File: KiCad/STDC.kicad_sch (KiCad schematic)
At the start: 20 parts, among them J1 TC2030, U1 STM32L476RGTx, X1 Q13FC1350000400

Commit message: Implement Comments, Working on PCB Layout
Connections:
- net Power+Battery/Batt_Status_SCL: now reaches U1.8 (PC0)
- net BAT_STATUS_HDQ renamed Power+Battery/Batt_Status_SDA
- no-connect marks 24 -> 23
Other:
- sheet Power+Battery ports: added Batt_Status_SCL, Batt_Status_SDA; removed BATT_STATUS_HDQ
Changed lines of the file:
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@@
 	)
 	(no_connect
-		(at 130.81 68.58)
-	)
-	(no_connect
 		(at 130.81 76.2)
 	)
@@
 	(wire
 		(pts
-			(xy 85.09 86.36) (xy 105.41 86.36)
+			(xy 85.09 86.36) (xy 106.68 86.36)
 		)
 		(stroke
@@
 	(wire
 		(pts
+			(xy 85.09 83.82) (xy 104.14 83.82)
+		)
+		(stroke
+			(width 0)
+			(type default)
+		)
+	)
+	(wire
+		(pts
 			(xy 130.81 106.68) (xy 119.38 106.68)
 		)
@@
 	(wire
 		(pts
-			(xy 130.81 88.9) (xy 85.09 88.9)
+			(xy 85.09 88.9) (xy 130.81 88.9)
 		)
 		(stroke
@@
 	(wire
 		(pts
-			(xy 105.41 71.12) (xy 130.81 71.12)
+			(xy 106.68 71.12) (xy 130.81 71.12)
 		)
 		(stroke
@@
 	(wire
 		(pts
-			(xy 105.41 86.36) (xy 105.41 71.12)
+			(xy 104.14 83.82) (xy 104.14 68.58)
+		)
+		(stroke
+			(width 0)
+			(type default)
+		)
+	)
+	(wire
+		(pts
+			(xy 106.68 86.36) (xy 106.68 71.12)
 		)
 		(stroke
@@
 	(wire
 		(pts
+			(xy 104.14 68.58) (xy 130.81 68.58)
+		)
+		(stroke
+			(width 0)
+			(type default)
+		)
+	)
+	(wire
+		(pts
 			(xy 82.55 34.29) (xy 92.71 34.29)
 		)
@@
 		)
 	)
-	(label "BAT_STATUS_HDQ"
-		(at 113.03 71.12 0)
-		(effects
-			(font
-				(size 1.27 1.27)
-			)
-			(justify left bottom)
-		)
-	)
 	(label "SWDCK"
 		(at 66.04 160.02 180)
@@
 	)
 	(sheet
-		(at 63.5 85.09)
-		(size 21.59 7.62)
+		(at 63.5 82.55)
+		(size 21.59 10.16)
 		(exclude_from_sim no)
 		(in_bom yes)
@@
 		)
 		(property "Sheetname" "Power+Battery"
-			(at 63.5 84.3784 0)
+			(at 63.5 81.8384 0)
 			(effects
 				(font
@@
 			)
 		)
-		(pin "BATT_STATUS_HDQ" input
-			(at 85.09 86.36 0)
+		(pin "{slash}RED_LED" input
+			(at 85.09 91.44 0)
 			(effects
 				(font
@@
 			)
 		)
-		(pin "{slash}RED_LED" input
-			(at 85.09 91.44 0)
+		(pin "{slash}BLUE_LED" input
+			(at 85.09 88.9 0)
 			(effects
 				(font
@@
 			)
 		)
-		(pin "{slash}BLUE_LED" input
-			(at 85.09 88.9 0)
+		(pin "Batt_Status_SCL" input
+			(at 85.09 83.82 0)
+			(effects
+				(font
+					(size 1.27 1.27)
+				)
+				(justify right)
+			)
+		)
+		(pin "Batt_Status_SDA" input
+			(at 85.09 86.36 0)
 			(effects
 				(font

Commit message: PCB Layout V0.1 with errors
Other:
- company: ETH Zurich: Center for Project Based Learning -> ETH Zürich: Center for Project Based Learning
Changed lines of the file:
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@@
 		(date "2026-03-09")
 		(rev "0.0.2")
-		(company "ETH Zurich: Center for Project Based Learning")
+		(company "ETH Zürich: Center for Project Based Learning")
 	)
 	(rectangle

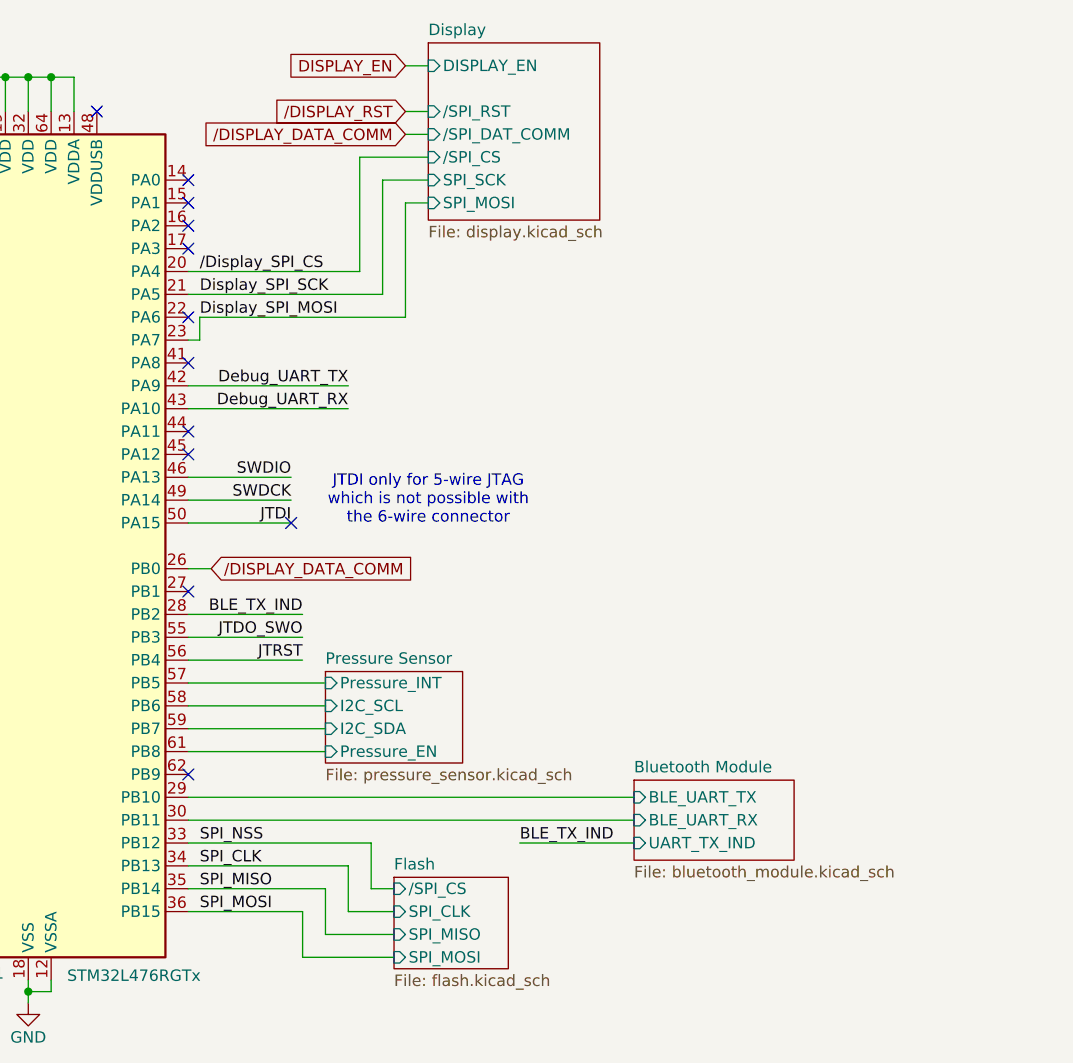
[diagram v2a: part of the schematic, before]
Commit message: V2 beginning with buttons, resistor, ...
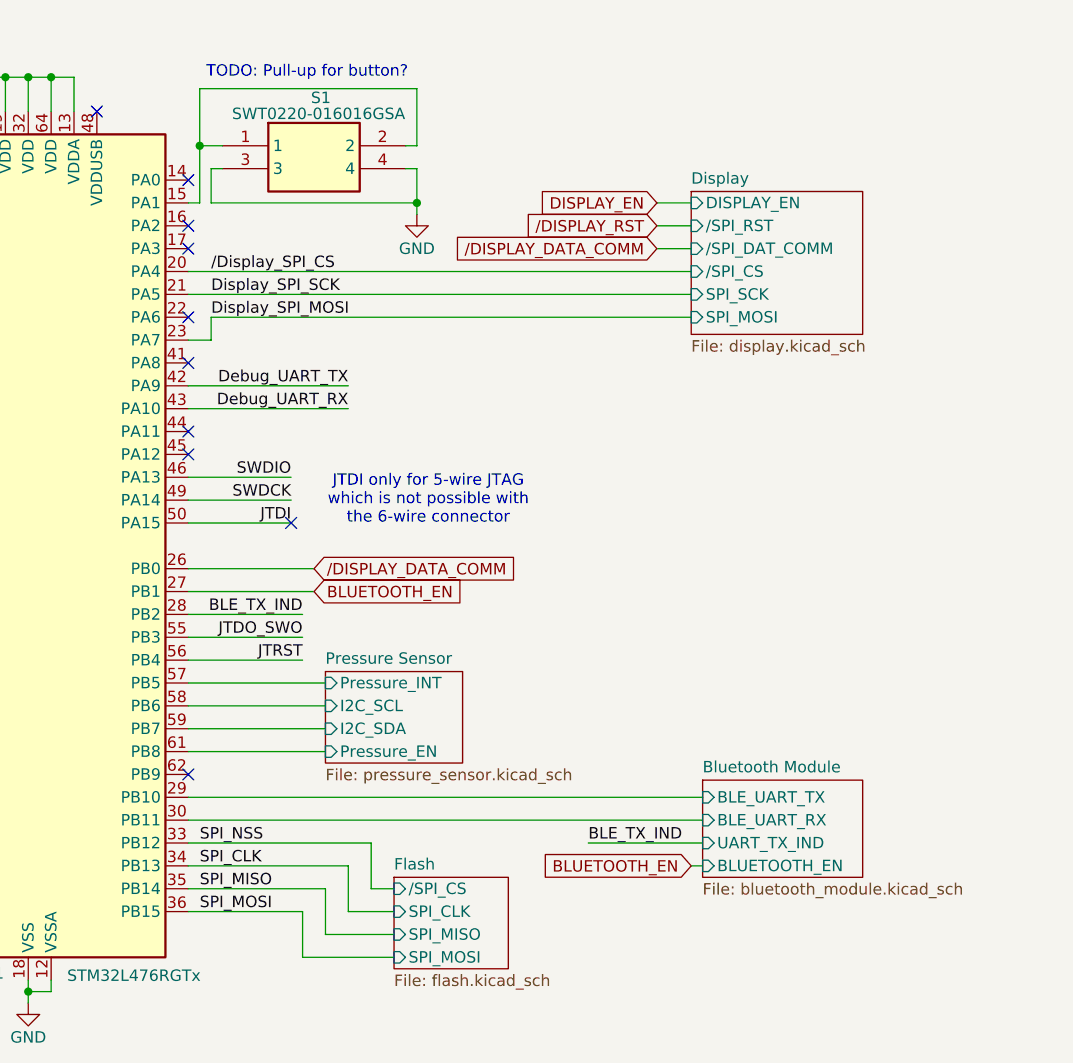
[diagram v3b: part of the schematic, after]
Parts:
- added S1: SWT0220-016016GSA, LIB_SWT0220-016016GSA:SWT0220016016GSA, symbol SWT SMD Button/Switch:SWT0220-016016GSA
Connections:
- net GND: now also S1.3, S1.4
- net at U1.15 (PA1): now also S1.1, S1.2
- net BLUETOOTH_EN: now reaches U1.27 (PB1)
- no-connect marks 23 -> 21
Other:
- sheet Bluetooth Module ports: added BLUETOOTH_EN; removed none
- note added: "TODO: Pull-up for button?"
